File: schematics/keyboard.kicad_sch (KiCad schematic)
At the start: 33 parts, among them J3 Mini-DIN-6, Q1 2N7000, Q3 2N7000, Q4 2N7000, Q5 2N7000, U1 74HC595, U13 ATF22V10C-7, U14 74HC14, U15 74HC280, U18 74HC04, U19 74HC00, U4 74HC595, U5 74HC165, U6 74HC165

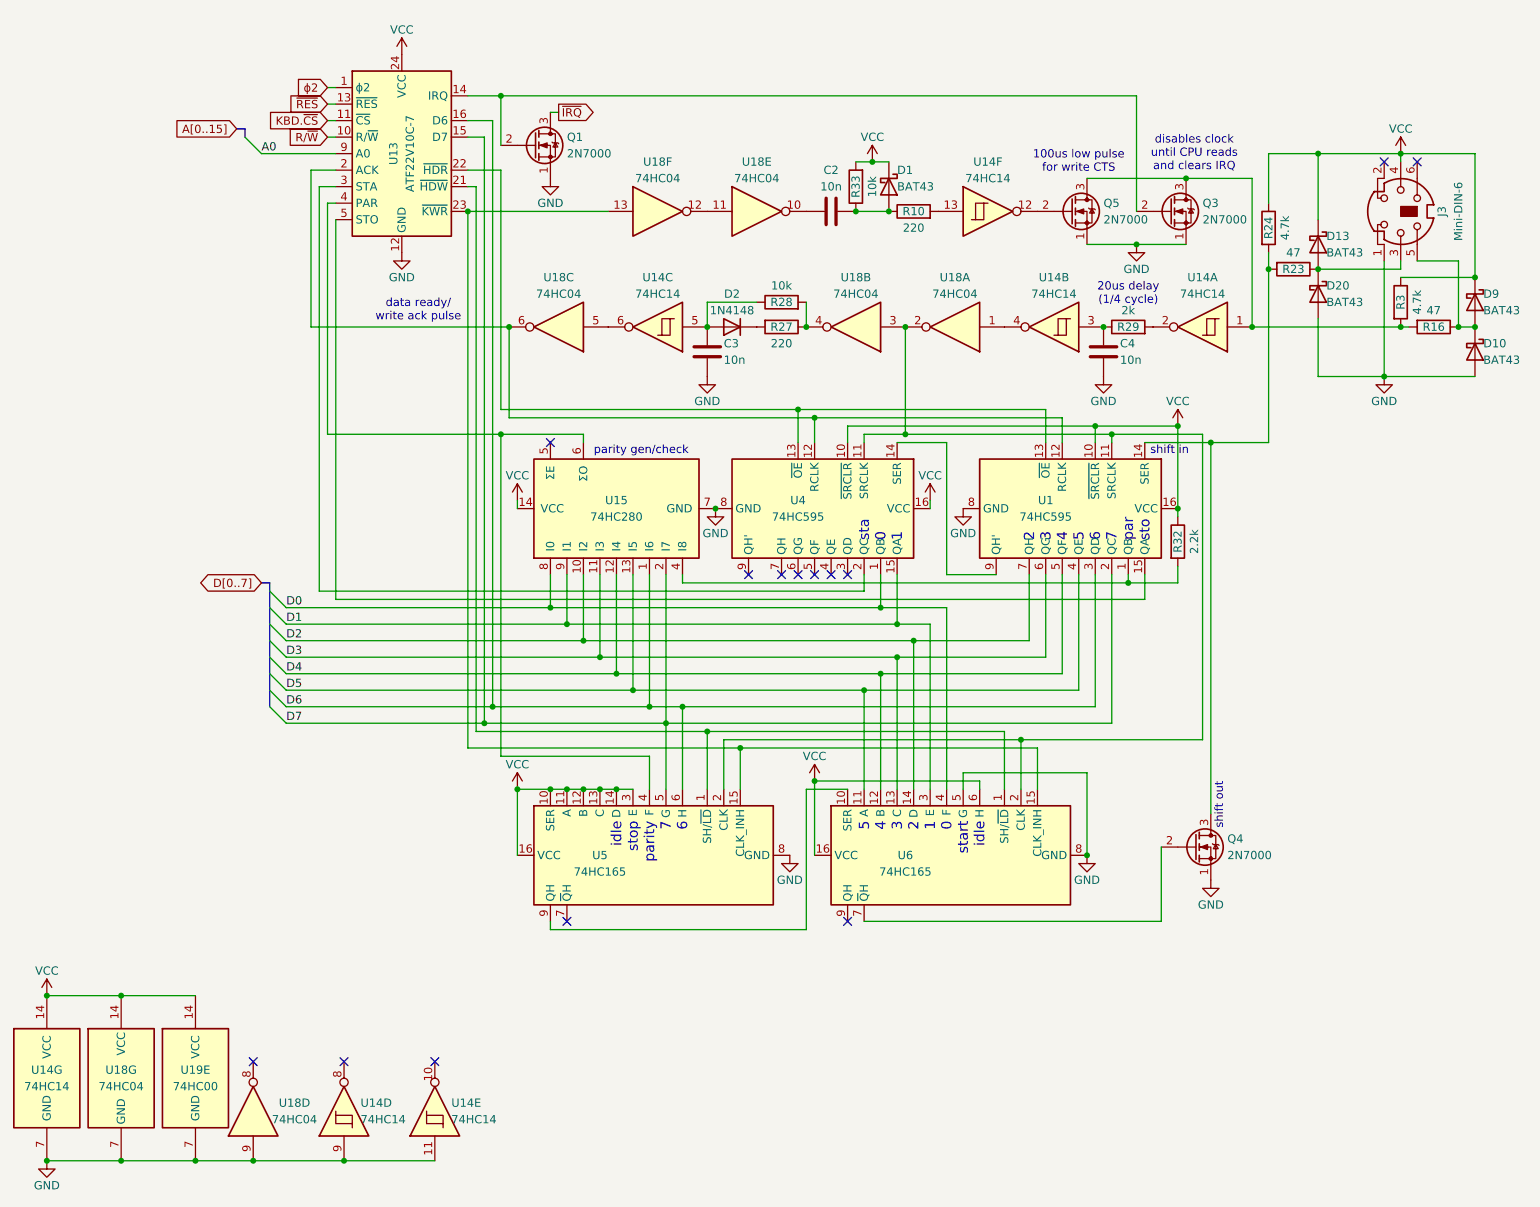
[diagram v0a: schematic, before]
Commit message: PLD files and schematics for address decoder, device selector, keyboard controller, lcd controller, banked memory, and bootloader.
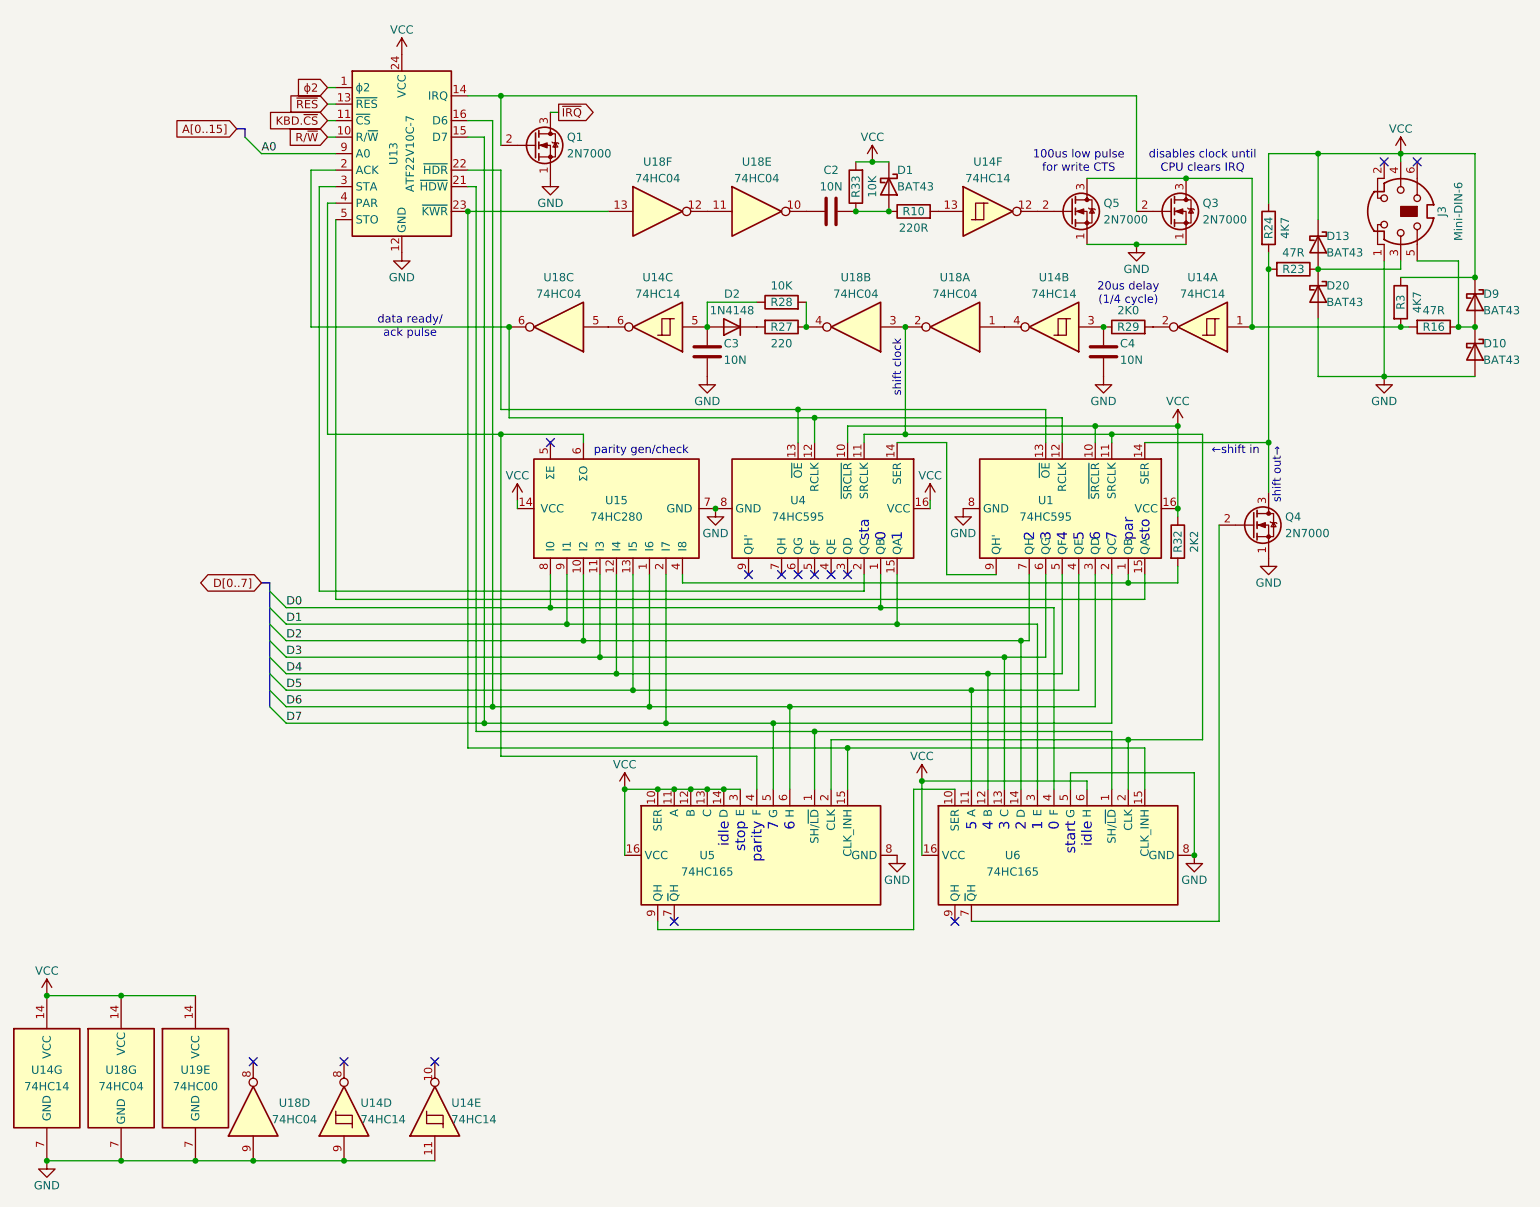
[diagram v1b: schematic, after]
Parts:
- C2, C3, C4: value 10n -> 10N
- R10: value 220 -> 220R
- R16, R23: value 47 -> 47R
- R24, R3: value 4.7k -> 4K7
- R28, R33: value 10k -> 10K
- R29: value 2k -> 2K0
- R32: value 2.2k -> 2K2
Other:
- note added: "data ready/ ack pulse"
- note added: "disables clock until CPU clears IRQ"
- note added: "shift clock"
- note added: "shift out→"
- note added: "←shift in"
- note removed: "data ready/ write ack pulse"
- note removed: "disables clock until CPU reads and clears IRQ"
- note removed: "shift in"
- note removed: "shift out"
- moved on the sheet: Q4, U5, U6

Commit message: keyboard, via, acia updates, ready to test
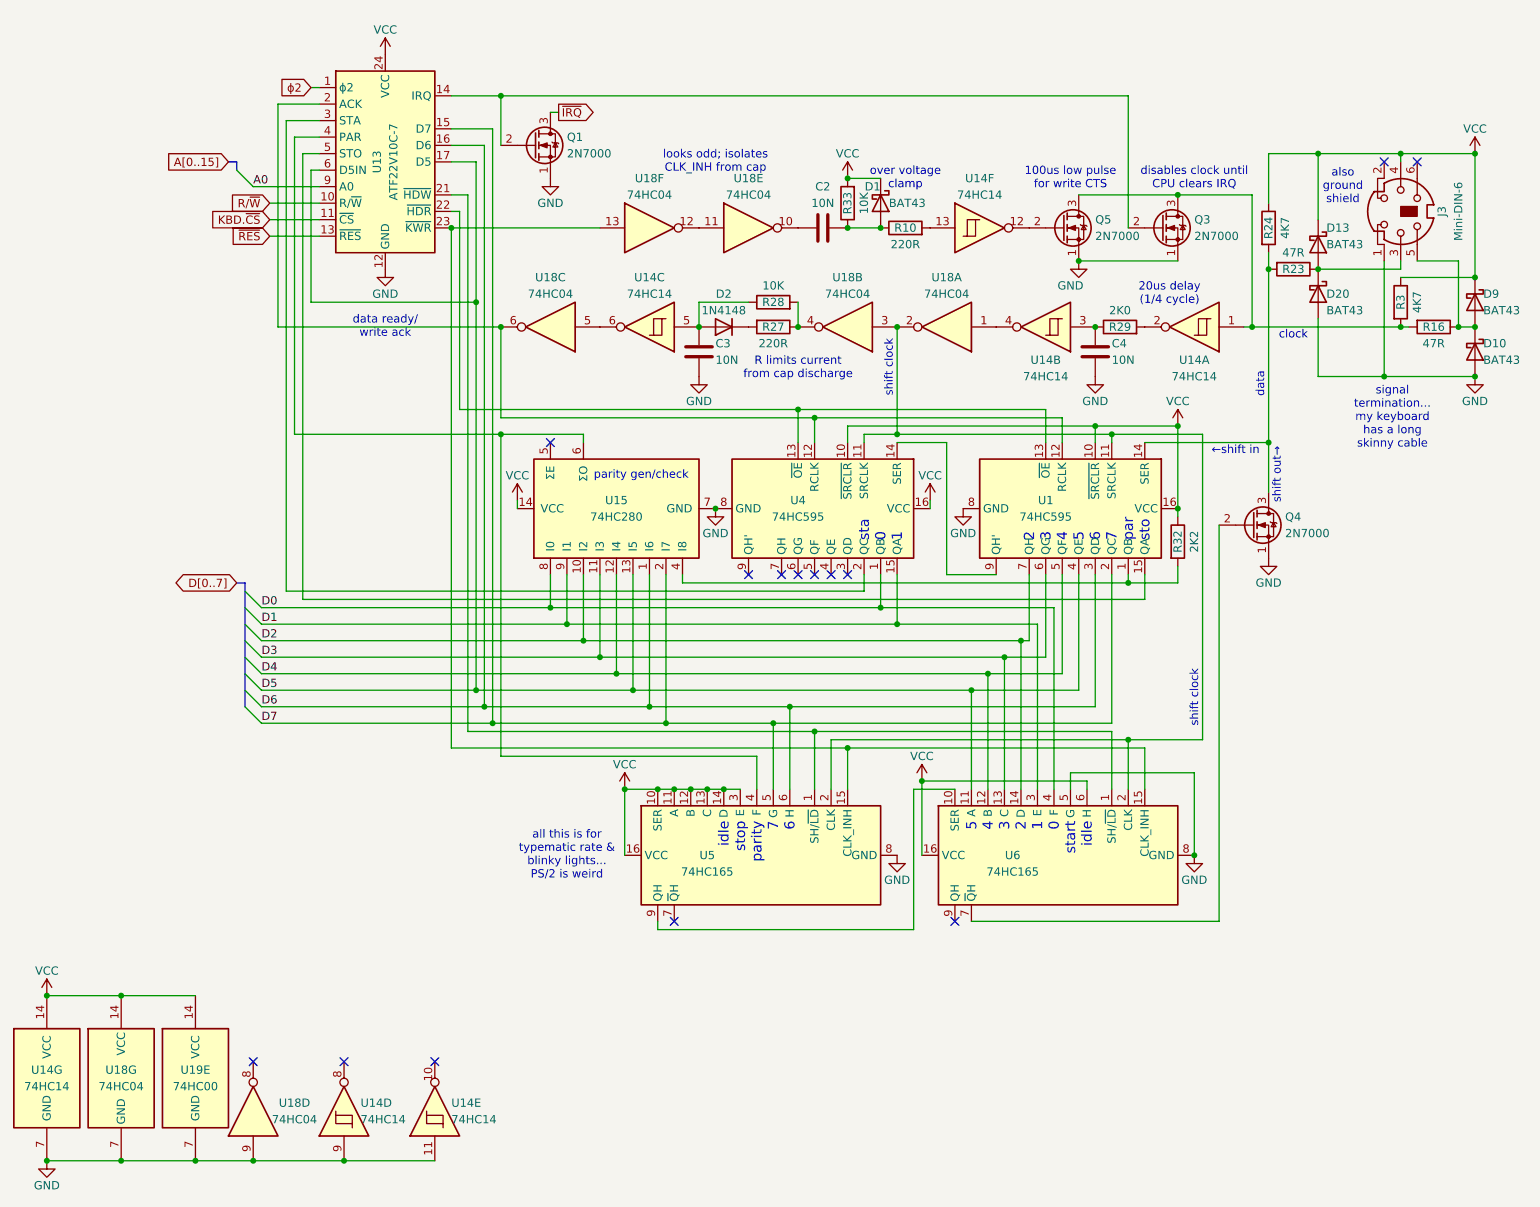
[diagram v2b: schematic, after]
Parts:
- R27: value 220 -> 220R
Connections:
- net D5: now also U13.17 (D5), U13.6 (D5IN)
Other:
- note added: "R limits current from cap discharge"
- note added: "all this is for typematic rate & blinky lights... PS/2 is weird"
- note added: "also ground shield"
- note added: "clock"
- note added: "data"
- note added: "data ready/ write ack"
- note added: "looks odd; isolates CLK_INH from cap"
- note added: "over voltage clamp"
- note added: "signal termination... my keyboard has a long skinny cable"
- note removed: "data ready/ ack pulse"
- moved on the sheet: C2, C3, C4, D1, D2, Q3, Q5, R10, R27, R28, R29, R33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

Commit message: added phi0 for write latch timing
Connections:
- net D5: now also U13.7 (D5IN); no longer U13.6 (D5IN)
- net VCC: no longer U13.24 (VCC)
- net ϕ2: now also U13.2 (ϕ2); no longer U13.1 (ϕ2)
- net at U1.12 (RCLK), U18.6, U4.12 (RCLK): now also U13.3 (ACK); no longer U13.2 (ACK)
- net at U4.2 (QC): now also U13.4 (STA); no longer U13.3 (STA)
- net at U15.6 (ΣO), U5.4 (F): now also U13.5 (PAR); no longer U13.4 (PAR)
- net at U1.15 (QA): now also U13.6 (STO); no longer U13.5 (STO)
- new net ϕ0: U13.1 (ϕ0)
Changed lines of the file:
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@@
 	(text "data ready/\nwrite ack"
 		(exclude_from_sim no)
-		(at 69.85 69.85 0)
+		(at 69.85 72.39 0)
 		(effects
 			(font
@@
 	)
 	(junction
-		(at 83.82 66.04)
-		(diameter 0)
-		(color 0 0 0 0)
-	)
-	(junction
 		(at 106.68 140.97)
 		(diameter 0)
@@
 	)
 	(junction
+		(at 83.82 67.31)
+		(diameter 0)
+		(color 0 0 0 0)
+	)
+	(junction
 		(at 179.07 69.85)
 		(diameter 0)
@@
 	)
 	(bus_entry
-		(at 46.99 45.72)
+		(at 46.99 46.99)
 		(size 2.54 2.54)
 		(stroke
@@
 	(wire
 		(pts
-			(xy 59.69 35.56) (xy 53.34 35.56)
+			(xy 59.69 36.83) (xy 53.34 36.83)
 		)
 		(stroke
@@
 	(wire
 		(pts
-			(xy 52.07 50.8) (xy 59.69 50.8)
+			(xy 52.07 52.07) (xy 59.69 52.07)
 		)
 		(stroke
@@
 	(wire
 		(pts
-			(xy 52.07 53.34) (xy 59.69 53.34)
+			(xy 52.07 54.61) (xy 59.69 54.61)
 		)
 		(stroke
@@
 	(wire
 		(pts
-			(xy 58.42 45.72) (xy 58.42 66.04)
+			(xy 58.42 46.99) (xy 58.42 67.31)
 		)
 		(stroke
@@
 	(wire
 		(pts
-			(xy 59.69 43.18) (xy 57.15 43.18)
+			(xy 59.69 44.45) (xy 57.15 44.45)
 		)
 		(stroke
@@
 	(wire
 		(pts
-			(xy 58.42 33.02) (xy 59.69 33.02)
+			(xy 58.42 34.29) (xy 59.69 34.29)
 		)
 		(stroke
@@
 	(wire
 		(pts
-			(xy 52.07 55.88) (xy 59.69 55.88)
+			(xy 52.07 57.15) (xy 59.69 57.15)
 		)
 		(stroke
@@
 	(wire
 		(pts
-			(xy 49.53 48.26) (xy 59.69 48.26)
+			(xy 49.53 49.53) (xy 59.69 49.53)
 		)
 		(stroke
@@
 	(wire
 		(pts
-			(xy 59.69 40.64) (xy 55.88 40.64)
+			(xy 59.69 41.91) (xy 55.88 41.91)
 		)
 		(stroke
@@
 	(bus
 		(pts
-			(xy 45.72 44.45) (xy 46.99 44.45)
+			(xy 45.72 45.72) (xy 46.99 45.72)
 		)
 		(stroke
@@
 	(bus
 		(pts
-			(xy 46.99 44.45) (xy 46.99 45.72)
+			(xy 46.99 45.72) (xy 46.99 46.99)
 		)
 		(stroke
@@
 	(wire
 		(pts
+			(xy 83.82 67.31) (xy 83.82 125.73)
+		)
+		(stroke
+			(width 0)
+			(type default)
+		)
+	)
+	(wire
+		(pts
 			(xy 140.97 140.97) (xy 140.97 134.62)
 		)
@@
 	(wire
 		(pts
-			(xy 59.69 45.72) (xy 58.42 45.72)
+			(xy 59.69 46.99) (xy 58.42 46.99)
 		)
 		(stroke
@@
 	(wire
 		(pts
+			(xy 83.82 44.45) (xy 83.82 67.31)
+		)
+		(stroke
+			(width 0)
+			(type default)
+		)
+	)
+	(wire
+		(pts
 			(xy 85.09 41.91) (xy 85.09 128.27)
 		)
@@
 	(wire
 		(pts
-			(xy 55.88 40.64) (xy 55.88 86.36)
+			(xy 55.88 41.91) (xy 55.88 86.36)
 		)
 		(stroke
@@
 	(wire
 		(pts
+			(xy 58.42 31.75) (xy 59.69 31.75)
+		)
+		(stroke
+			(width 0)
+			(type default)
+		)
+	)
+	(wire
+		(pts
 			(xy 234.95 59.69) (xy 234.95 69.85)
 		)
@@
 	(wire
 		(pts
-			(xy 54.61 38.1) (xy 59.69 38.1)
+			(xy 54.61 39.37) (xy 59.69 39.37)
 		)
 		(stroke
@@
 	(wire
 		(pts
-			(xy 57.15 43.18) (xy 57.15 111.76)
+			(xy 57.15 44.45) (xy 57.15 111.76)
 		)
 		(stroke
@@
 	(wire
 		(pts
-			(xy 54.61 110.49) (xy 54.61 38.1)
+			(xy 54.61 110.49) (xy 54.61 39.37)
 		)
 		(stroke
@@
 	(wire
 		(pts
-			(xy 58.42 66.04) (xy 83.82 66.04)
+			(xy 58.42 67.31) (xy 83.82 67.31)
 		)
 		(stroke
@@
 	(wire
 		(pts
-			(xy 83.82 44.45) (xy 83.82 66.04)
-		)
-		(stroke
-			(width 0)
-			(type default)
-		)
-	)
-	(wire
-		(pts
 			(xy 237.49 62.23) (xy 237.49 43.18)
 		)
@@
 	(wire
 		(pts
-			(xy 53.34 35.56) (xy 53.34 69.85)
+			(xy 53.34 36.83) (xy 53.34 69.85)
 		)
 		(stroke
@@
 	(wire
 		(pts
-			(xy 83.82 66.04) (xy 83.82 125.73)
-		)
-		(stroke
-			(width 0)
-			(type default)
-		)
-	)
-	(wire
-		(pts
 			(xy 85.09 128.27) (xy 110.49 128.27)
 		)
@@
 	)
 	(label "A0"
-		(at 49.53 48.26 0)
+		(at 49.53 49.53 0)
 		(effects
 			(font
@@
 	(global_label "~{RES}"
 		(shape input)
-		(at 52.07 55.88 180)
+		(at 52.07 57.15 180)
 		(fields_autoplaced yes)
 		(effects
@@
 		)
 		(property "Intersheetrefs" "${INTERSHEET_REFS}"
-			(at 45.4563 55.88 0)
+			(at 45.4563 57.15 0)
 			(hide yes)
 			(show_name no)
@@
 	(global_label "R{slash}~{W}"
 		(shape input)
-		(at 52.07 50.8 180)
+		(at 52.07 52.07 180)
 		(fields_autoplaced yes)
 		(effects
@@
 		)
 		(property "Intersheetrefs" "${INTERSHEET_REFS}"
-			(at 45.0329 50.8 0)
+			(at 45.0329 52.07 0)
 			(hide yes)
 			(show_name no)
@@
 	(global_label "ϕ2"
 		(shape input)
-		(at 58.42 33.02 180)
+		(at 58.42 34.29 180)
 		(fields_autoplaced yes)
 		(effects
@@
 		)
 		(property "Intersheetrefs" "${INTERSHEET_REFS}"
-			(at 52.8948 33.02 0)
+			(at 52.8948 34.29 0)
 			(hide yes)
 			(show_name no)
@@
 	(global_label "KBD.~{CS}"
 		(shape input)
-		(at 52.07 53.34 180)
+		(at 52.07 54.61 180)
 		(fields_autoplaced yes)
 		(effects
@@
 		)
 		(property "Intersheetrefs" "${INTERSHEET_REFS}"
-			(at 42.1905 53.34 0)
+			(at 42.1905 54.61 0)
 			(hide yes)
 			(show_name no)
@@
 	(global_label "A[0..15]"
 		(shape input)
-		(at 45.72 44.45 180)
+		(at 45.72 45.72 180)
+		(fields_autoplaced yes)
+		(effects
+			(font
+				(size 1.27 1.27)
+			)
+			(justify right)
+		)
+		(property "Intersheetrefs" "${INTERSHEET_REFS}"
+			(at 35.1147 45.72 0)
+			(hide yes)
+			(show_name no)
+			(do_not_autoplace no)
+			(effects
+				(font
+					(size 1.27 1.27)
+				)
+				(justify right)
+			)
+		)
+	)
+	(global_label "ϕ0"
+		(shape input)
+		(at 58.42 31.75 180)
 		(fields_autoplaced yes)
 		(effects
@@
 		)
 		(property "Intersheetrefs" "${INTERSHEET_REFS}"
-			(at 35.1147 44.45 0)
+			(at 52.8948 31.75 0)
 			(hide yes)
 			(show_name no)
@@
 	(symbol
 		(lib_id "power:GND")
-		(at 69.85 60.96 0)
+		(at 69.85 62.23 0)
 		(unit 1)
 		(body_style 1)
@@
 		(dnp no)
 		(property "Reference" "#PWR037"
-			(at 69.85 67.31 0)
+			(at 69.85 68.58 0)
 			(hide yes)
 			(show_name no)
@@
 		)
 		(property "Value" "GND"
-			(at 69.85 64.77 0)
+			(at 69.85 66.04 0)
 			(show_name no)
 			(do_not_autoplace no)
@@
 		)
 		(property "Footprint" ""
-			(at 69.85 60.96 0)
+			(at 69.85 62.23 0)
 			(hide yes)
 			(show_name no)
@@
 		)
 		(property "Datasheet" ""
-			(at 69.85 60.96 0)
+			(at 69.85 62.23 0)
 			(hide yes)
 			(show_name no)
@@
 		)
 		(property "Description" "Power symbol creates a global label with name \"GND\" , ground"
-			(at 69.85 60.96 0)
+			(at 69.85 62.23 0)
 			(hide yes)
 			(show_name no)
